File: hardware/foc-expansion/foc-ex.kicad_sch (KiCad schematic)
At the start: 4 parts, among them J1 Conn_01x02, SW1 SW_Push, U1 ESP32-S3-WROOM-1

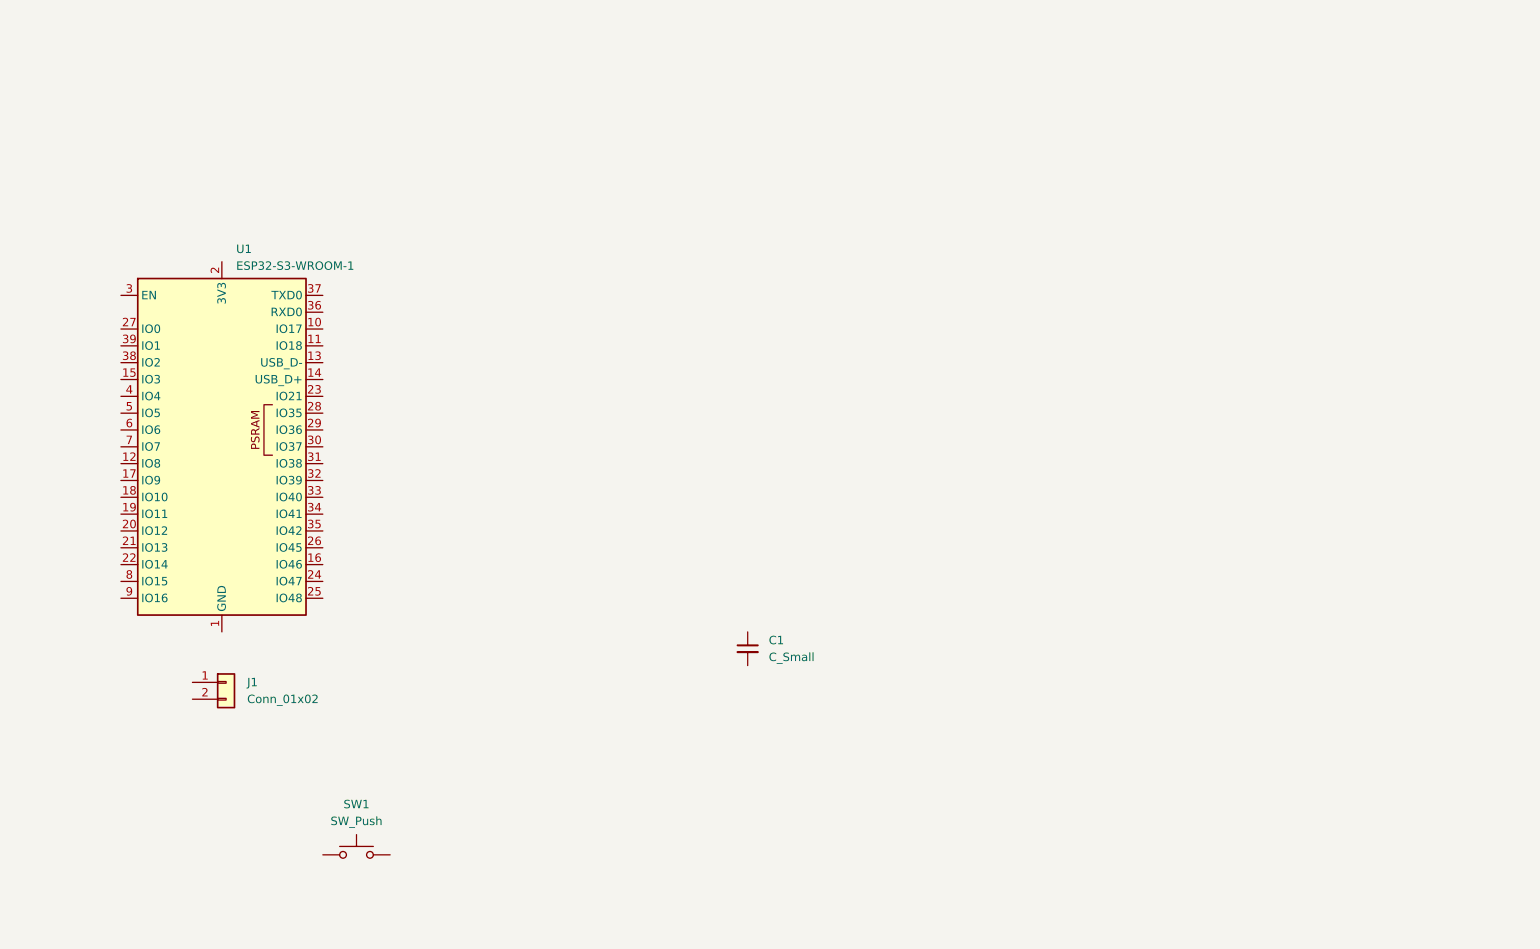
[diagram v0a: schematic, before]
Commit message: feat: integrate FOC host tooling and wireless control stack
- add the Vue/Tauri desktop app, device sessions and transport adapters
- add the shared v2 wire protocol and firmware control-lease handling
- replace the PlatformIO bridge with native ESP-IDF PC/motor bridges
- capture drive-board and expansion-board design updates
- document setup, simulation limits and pending board validation
- exclude KiCad recovery files and preserve local editor state

Validation: 105 firmware tests, 14 host workspace tests, 7 wire tests,
bridge C++ interface tests, frontend production build, and encoder/Hall
ARM release builds and Clippy checks passed. No board validation performed.

Co-Authored-By: Claude Fable 5 <noreply@anthropic.com>
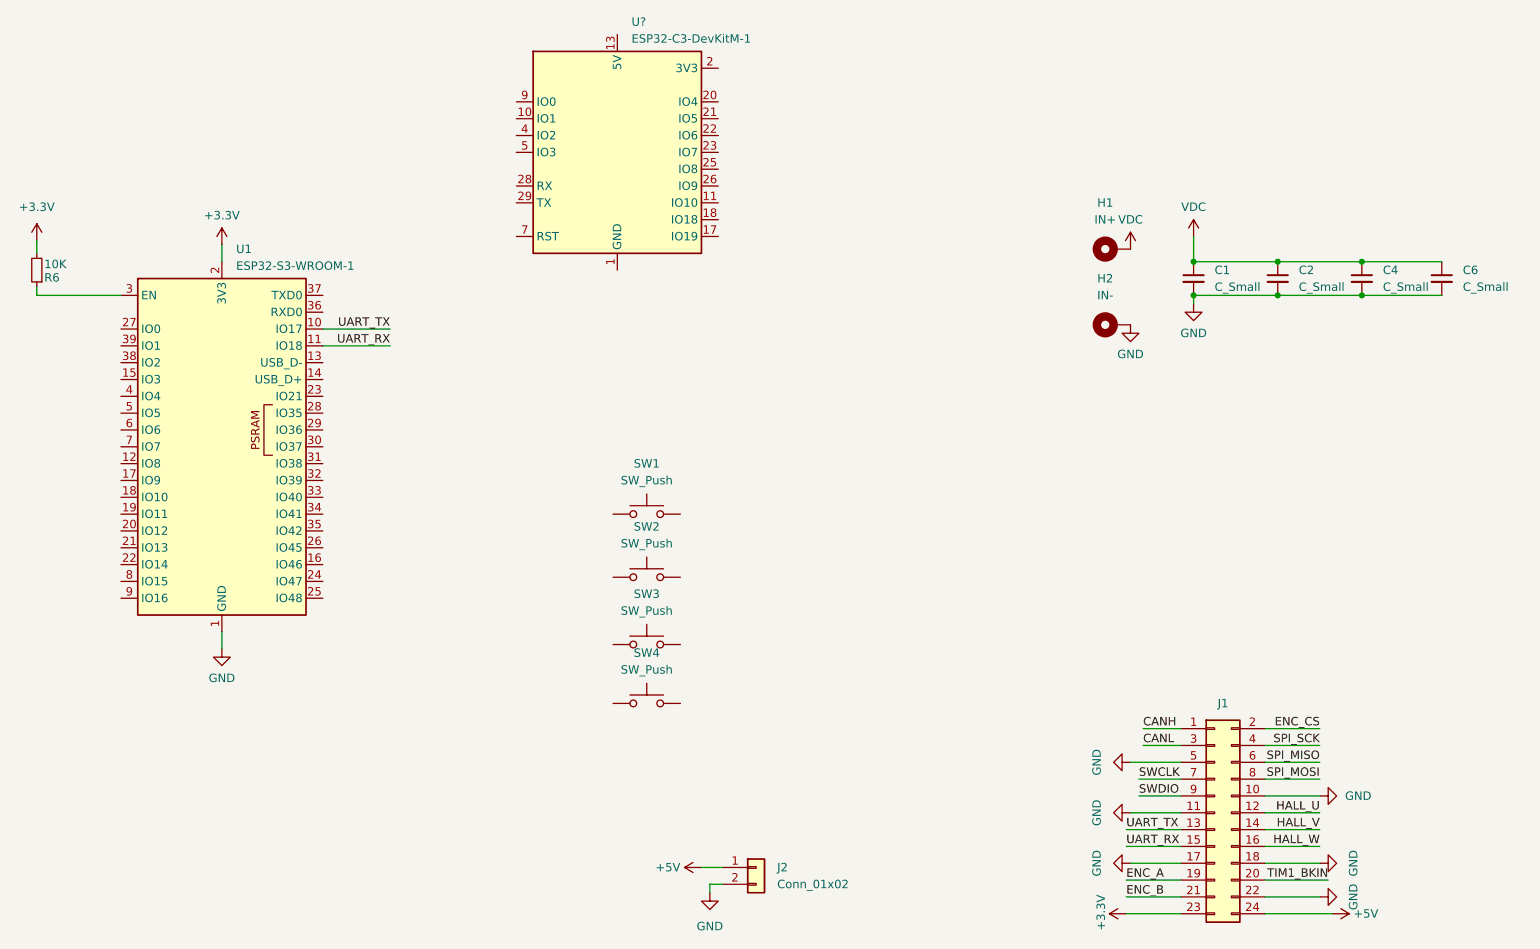
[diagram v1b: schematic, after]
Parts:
- added C2, C4, C6: C_Small, Capacitor_THT:CP_Radial_D6.3mm_P2.50mm, symbol Device:C_Small
- added H1: IN+, MountingHole:MountingHole_3.2mm_M3_ISO7380_Pad, symbol FOCLibrary:MountingHole_Pad
- added H2: IN-, MountingHole:MountingHole_3.2mm_M3_ISO7380_Pad, symbol FOCLibrary:MountingHole_Pad
- added J1: Conn_02x12_Odd_Even, Connector_PinHeader_2.54mm:PinHeader_2x12_P2.54mm_Vertical, symbol Connector_Generic:Conn_02x12_Odd_Even
- added R6: 10K, Resistor_SMD:R_0603_1608Metric, symbol Device:R_Small
- added SW2, SW3, SW4: SW_Push, Button_Switch_SMD:SW_Push_SPST_NO_Alps_SKRK, symbol Switch:SW_Push
- added U?: ESP32-C3-DevKitM-1, RF_Module:ESP32-C3-DevKitM-1, symbol RF_Module:ESP32-C3-DevKitM-1
- J2: renamed from J1; footprint Connector_PinHeader_2.54mm:PinHeader_1x02_P2.54mm_Vertical -> Connector_JST:JST_XH_B2B-XH-A_1x02_P2.50mm_Vertical
- SW1: footprint Button_Switch_THT:SW_PUSH_6mm -> Button_Switch_SMD:SW_Push_SPST_NO_Alps_SKRK
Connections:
- net +5V: now reaches J2.1 (Pin_1)
- net +5V: now also J1.24 (Pin_24)
- net GND: now reaches J2.2 (Pin_2)
- net GND: now also C1.2, U1.1 (GND), U1.40 (GND), U1.41 (GND), C2.2, C4.2, C6.2, H2.1, J1.10 (Pin_10), J1.11 (Pin_11), J1.17 (Pin_17), J1.18 (Pin_18), J1.22 (Pin_22), J1.5 (Pin_5)
- net UART_TX: now reaches U1.10 (IO17)
- net UART_TX: now also J1.13 (Pin_13)
- net UART_RX: now reaches U1.11 (IO18)
- net UART_RX: now also J1.15 (Pin_15)
- net +3.3V: now reaches U1.2 (3V3)
- net +3.3V: now also J1.23 (Pin_23), R6.2
- net at U1.3 (EN): now also R6.1
- net VDC: now reaches C1.1
- net VDC: now also C2.1, C4.1, C6.1, H1.1
- new net: U?.1 (GND), U?.12 (GND), U?.15 (GND), U?.16 (GND), U?.19 (GND), U?.24 (GND), U?.27 (GND), U?.30 (GND), U?.6 (GND), U?.8 (GND)
- new net: U?.13 (5V), U?.14 (5V)
- new net: U?.2 (3V3), U?.3 (3V3)
- new net CANH: J1.1 (Pin_1)
- new net CANL: J1.3 (Pin_3)
- new net ENC_A: J1.19 (Pin_19)
- new net ENC_B: J1.21 (Pin_21)
- new net ENC_CS: J1.2 (Pin_2)
- new net HALL_U: J1.12 (Pin_12)
- new net HALL_V: J1.14 (Pin_14)
- new net HALL_W: J1.16 (Pin_16)
- new net SPI_MISO: J1.6 (Pin_6)
- new net SPI_MOSI: J1.8 (Pin_8)
- new net SPI_SCK: J1.4 (Pin_4)
- new net SWCLK: J1.7 (Pin_7)
- new net SWDIO: J1.9 (Pin_9)
- new net TIM1_BKIN: J1.20 (Pin_20)
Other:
- moved on the sheet: C1, J2, SW1
